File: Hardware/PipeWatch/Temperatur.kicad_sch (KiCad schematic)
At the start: 2 parts

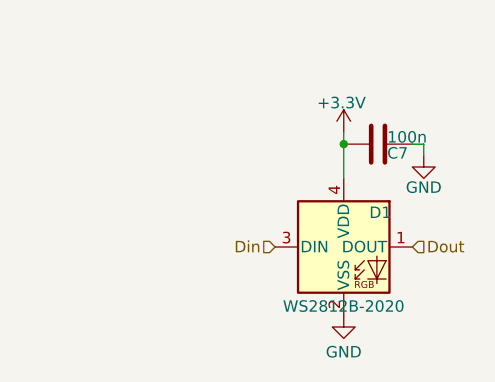
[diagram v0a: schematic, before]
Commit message: Added Ten Sensor
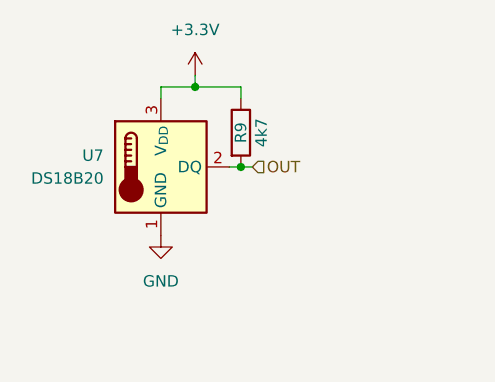
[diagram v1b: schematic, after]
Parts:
- removed C7: 100n, Capacitor_SMD:C_0603_1608Metric, symbol Device:C
- removed D1: WS2812B-2020, Felix:LED_4691_Neopixel_Edge, symbol LED:WS2812B-2020
- added R9: 4k7, Resistor_SMD:R_0603_1608Metric, symbol Device:R
- added U7: DS18B20, Package_TO_SOT_THT:TO-92_Inline, symbol Sensor_Temperature:DS18B20
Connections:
- net +3.3V: now also R9.1, U7.3 (V_{DD})
- net GND: now also U7.1 (GND)
- new net OUT: R9.2, U7.2 (DQ)

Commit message: Changed the scematic page Labeling
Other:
- company: (none) -> Felix Pelster
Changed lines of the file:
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@@
 	(generator_version "9.0")
 	(paper "A4")
+	(title_block
+		(date "2025-09-24")
+		(company "Felix Pelster")
+	)
 	(junction
 		(at 127 100.33)
